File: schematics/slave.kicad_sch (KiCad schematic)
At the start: 6 parts, among them SW1 SW_SPDT, U1 LF33_TO220, U2 ESP32-C6-DevKitC-1

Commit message: add a backup ir sensor
Signed-off-by: zayats1 <zaiats.bogdan@gmail.com>
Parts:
- added U3: IRM-H6xxT, OptoDevice:Everlight_IRM-H6xxT, symbol Interface_Optical:IRM-H6xxT
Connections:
- net +3.3V: now also U3.4 (Vcc)
- net at U2.23 (GPIO18): now also U3.3 (OUT)
- net at U2.32 (GND): now also U3.1 (GND), U3.2 (GND)
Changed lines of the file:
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@@
+	(wire
+		(pts
+			(xy 193.04 86.36) (xy 185.42 86.36)
+		)
+		(stroke
+			(width 0)
+			(type default)
+		)
+	)
 	(wire
 		(pts
@@
 	(wire
 		(pts
+			(xy 182.88 62.23) (xy 182.88 66.04)
+		)
+		(stroke
+			(width 0)
+			(type default)
+		)
+	)
+	(wire
+		(pts
 			(xy 142.24 43.18) (xy 127 43.18)
 		)
@@
 	(wire
 		(pts
+			(xy 182.88 71.12) (xy 207.01 71.12)
+		)
+		(stroke
+			(width 0)
+			(type default)
+		)
+	)
+	(wire
+		(pts
 			(xy 161.29 29.21) (xy 161.29 34.29)
 		)
@@
 	(wire
 		(pts
+			(xy 207.01 109.22) (xy 185.42 109.22)
+		)
+		(stroke
+			(width 0)
+			(type default)
+		)
+	)
+	(wire
+		(pts
+			(xy 182.88 76.2) (xy 193.04 76.2)
+		)
+		(stroke
+			(width 0)
+			(type default)
+		)
+	)
+	(wire
+		(pts
 			(xy 127 121.92) (xy 134.62 121.92)
 		)
@@
 	(wire
 		(pts
+			(xy 193.04 76.2) (xy 193.04 86.36)
+		)
+		(stroke
+			(width 0)
+			(type default)
+		)
+	)
+	(wire
+		(pts
 			(xy 161.29 41.91) (xy 161.29 43.18)
 		)
@@
 		(pts
 			(xy 127 128.27) (xy 127 121.92)
+		)
+		(stroke
+			(width 0)
+			(type default)
+		)
+	)
+	(wire
+		(pts
+			(xy 207.01 71.12) (xy 207.01 109.22)
 		)
 		(stroke
@@
 	)
 	(symbol
+		(lib_id "Interface_Optical:IRM-H6xxT")
+		(at 172.72 71.12 0)
+		(unit 1)
+		(exclude_from_sim no)
+		(in_bom yes)
+		(on_board yes)
+		(dnp no)
+		(fields_autoplaced yes)
+		(property "Reference" "U3"
+			(at 170.985 59.69 0)
+			(effects
+				(font
+					(size 1.27 1.27)
+				)
+			)
+		)
+		(property "Value" "IRM-H6xxT"
+			(at 170.985 62.23 0)
+			(effects
+				(font
+					(size 1.27 1.27)
+				)
+			)
+		)
+		(property "Footprint" "OptoDevice:Everlight_IRM-H6xxT"
+			(at 171.45 80.645 0)
+			(effects
+				(font
+					(size 1.27 1.27)
+				)
+				(hide yes)
+			)
+		)
+		(property "Datasheet" "https://en.everlight.com/wp-content/plugins/ItemRelationship/product_files/pdf/DMO-0000004-IRM-H6XX-TR2_Series_Datasheet_V4.pdf"
+			(at 189.23 63.5 0)
+			(effects
+				(font
+					(size 1.27 1.27)
+				)
+				(hide yes)
+			)
+		)
+		(property "Description" "IR Receiver Modules for remote controls"
+			(at 172.72 71.12 0)
+			(effects
+				(font
+					(size 1.27 1.27)
+				)
+				(hide yes)
+			)
+		)
+		(pin "3"
+		)
+		(pin "1"
+		)
+		(pin "2"
+		)
+		(pin "4"
+		)
+		(instances
+			(project ""
+				(path "/b33adb57-441b-4653-995a-012b7a2cdd51"
+					(reference "U3")
+					(unit 1)
+				)
+			)
+		)
+	)
+	(symbol
 		(lib_id "power:+3.3V")
 		(at 123.19 66.04 0)
@@
 					(unit 1)
 				)
+			)
+		)
+	)
+	(symbol
+		(lib_id "power:+3.3V")
+		(at 182.88 62.23 0)
+		(unit 1)
+		(exclude_from_sim no)
+		(in_bom yes)
+		(on_board yes)
+		(dnp no)
+		(fields_autoplaced yes)
+		(property "Reference" "#PWR02"
+			(at 182.88 66.04 0)
+			(effects
+				(font
+					(size 1.27 1.27)
+				)
+				(hide yes)
+			)
+		)
+		(property "Value" "+3.3V"
+			(at 182.88 57.15 0)
+			(effects
+				(font
+					(size 1.27 1.27)
+				)
+			)
+		)
+		(property "Footprint" ""
+			(at 182.88 62.23 0)
+			(effects
+				(font
+					(size 1.27 1.27)
+				)
+				(hide yes)
+			)
+		)
+		(property "Datasheet" ""
+			(at 182.88 62.23 0)
+			(effects
+				(font
+					(size 1.27 1.27)
+				)
+				(hide yes)
+			)
+		)
+		(property "Description" "Power symbol creates a global label with name \"+3.3V\""
+			(at 182.88 62.23 0)
+			(effects
+				(font
+					(size 1.27 1.27)
+				)
+				(hide yes)
+			)
+		)
+		(pin "1"
+		)
+		(instances
+			(project ""
+				(path "/b33adb57-441b-4653-995a-012b7a2cdd51"
+					(reference "#PWR02")
+					(unit 1)
+				)

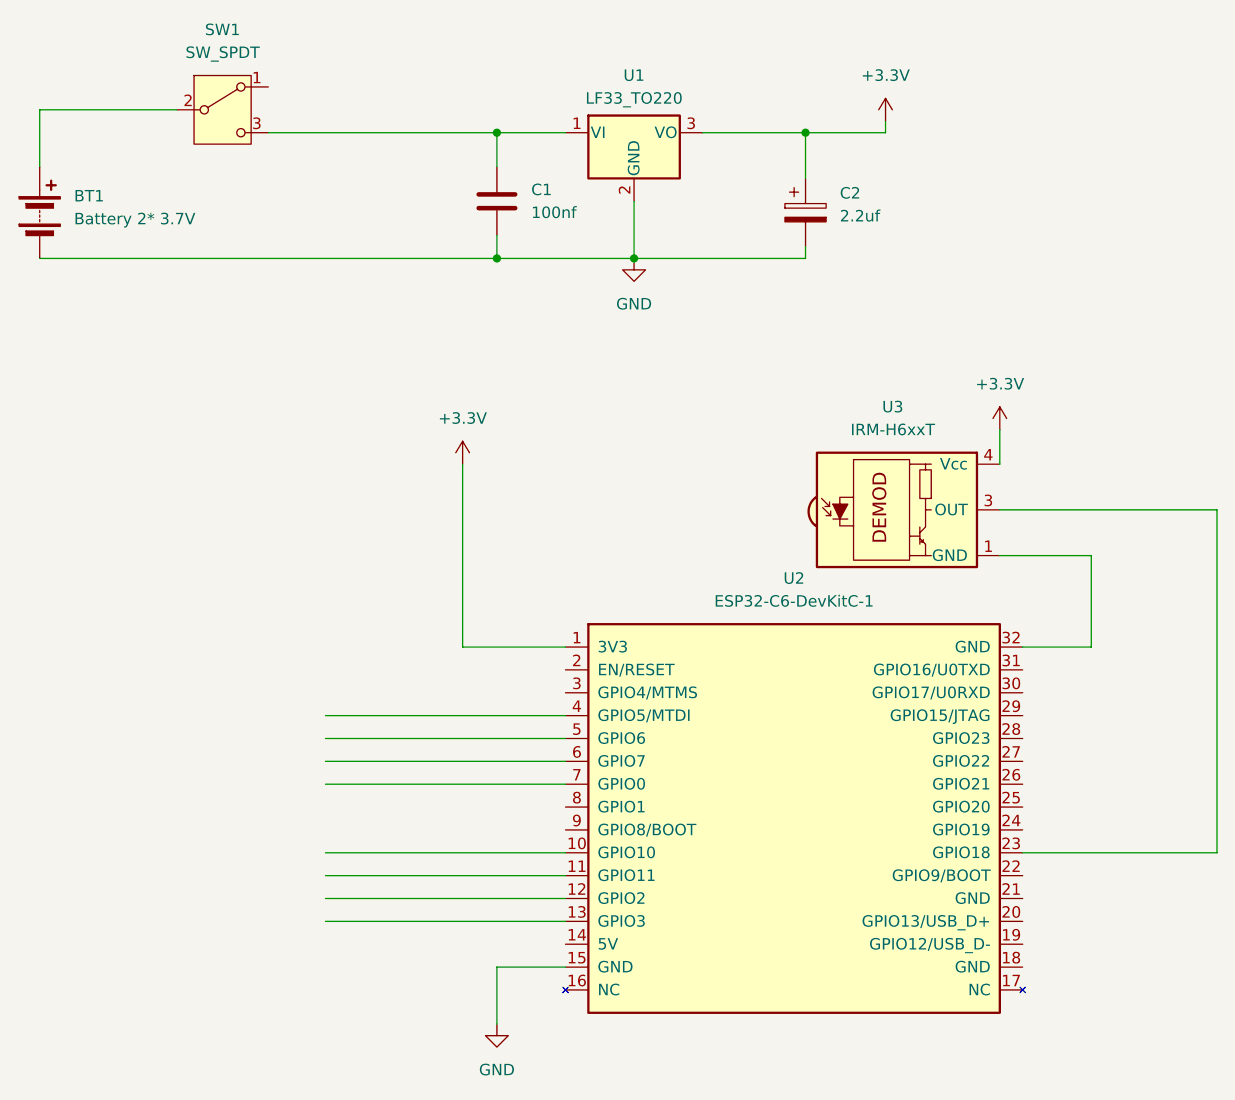
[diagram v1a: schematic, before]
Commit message: change voltage regulator IC to AMS1117-3.3 module
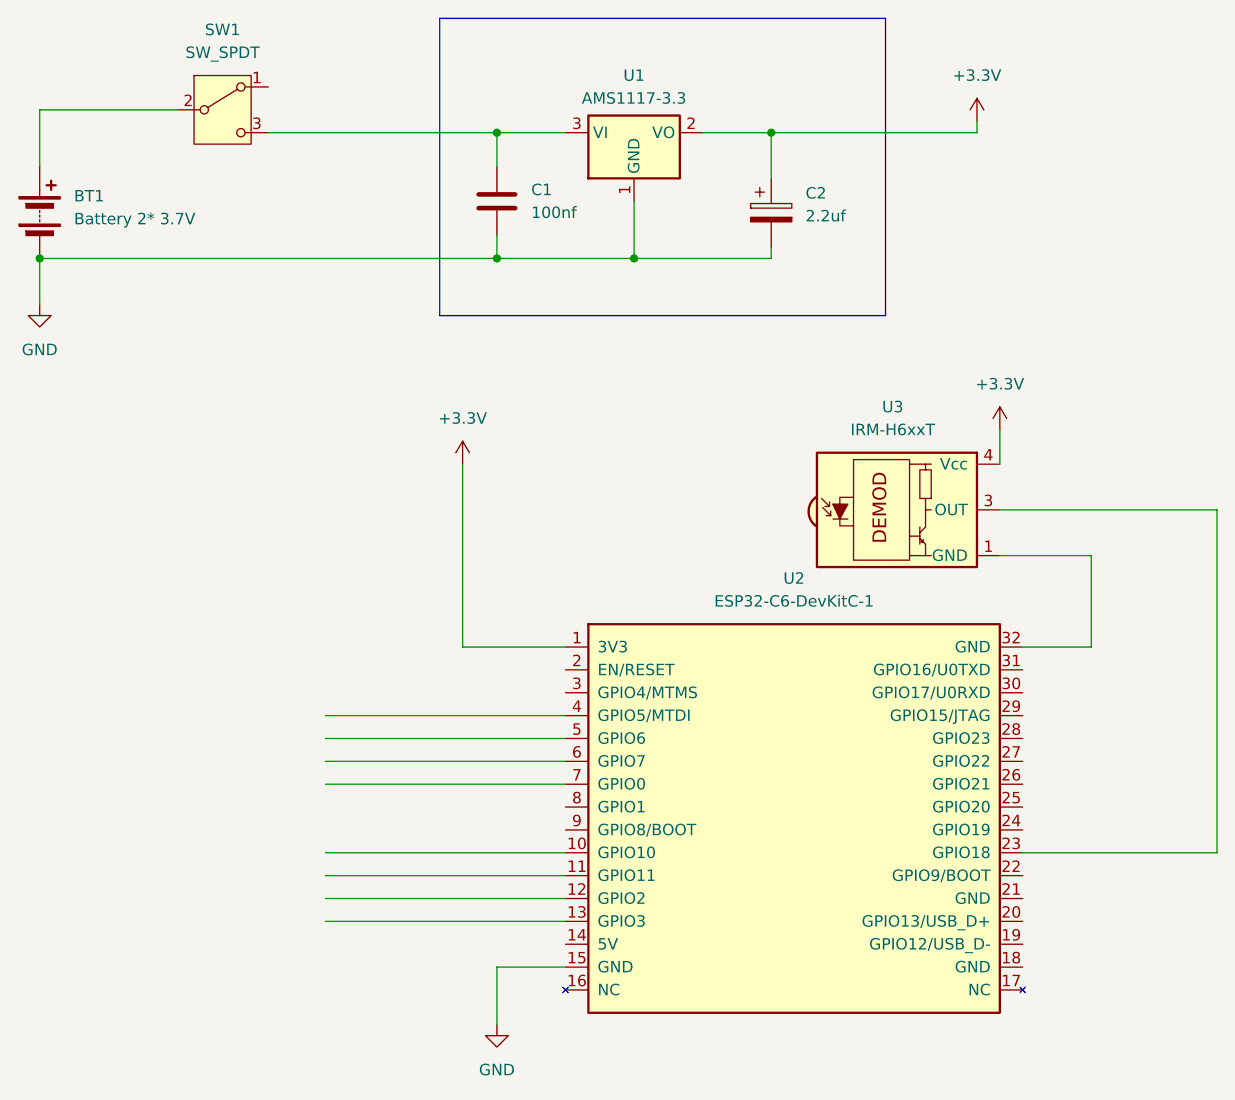
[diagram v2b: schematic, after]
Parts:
- removed U1: LF33_TO220, Package_TO_SOT_THT:TO-220-3_Vertical, symbol Regulator_Linear:LF33_TO220
- added U1: AMS1117-3.3, Package_TO_SOT_SMD:SOT-223-3_TabPin2, symbol Regulator_Linear:AMS1117-3.3
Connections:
- net +3.3V: now also U1.2 (VO)
- net GND: now also U1.1 (GND)
- net at C1.1, SW1.3 (C): now also U1.3 (VI)
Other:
- moved on the sheet: C2
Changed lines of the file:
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@@
 	(generator_version "9.0")
 	(paper "A4")
+	(rectangle
+		(start 120.65 16.51)
+		(end 170.18 49.53)
+		(stroke
+			(width 0)
+			(type default)
+		)
+		(fill
+			(type none)
+		)
+	)
 	(junction
-		(at 161.29 29.21)
+		(at 76.2 43.18)
 		(diameter 0)
 		(color 0 0 0 0)
@@
 		(color 0 0 0 0)
 	)
+	(junction
+		(at 157.48 29.21)
+		(diameter 0)
+		(color 0 0 0 0)
+	)
 	(wire
 		(pts
@@
 	(wire
 		(pts
+			(xy 76.2 43.18) (xy 76.2 48.26)
+		)
+		(stroke
+			(width 0)
+			(type default)
+		)
+	)
+	(wire
+		(pts
 			(xy 107.95 109.22) (xy 134.62 109.22)
 		)
@@
 	(wire
 		(pts
+			(xy 157.48 29.21) (xy 180.34 29.21)
+		)
+		(stroke
+			(width 0)
+			(type default)
+		)
+	)
+	(wire
+		(pts
 			(xy 76.2 26.67) (xy 91.44 26.67)
 		)
@@
 	(wire
 		(pts
-			(xy 161.29 29.21) (xy 170.18 29.21)
-		)
-		(stroke
-			(width 0)
-			(type default)
-		)
-	)
-	(wire
-		(pts
 			(xy 107.95 114.3) (xy 134.62 114.3)
 		)
@@
 	(wire
 		(pts
+			(xy 76.2 43.18) (xy 127 43.18)
+		)
+		(stroke
+			(width 0)
+			(type default)
+		)
+	)
+	(wire
+		(pts
 			(xy 182.88 71.12) (xy 207.01 71.12)
 		)
@@
 	(wire
 		(pts
-			(xy 161.29 29.21) (xy 161.29 34.29)
+			(xy 157.48 29.21) (xy 157.48 34.29)
 		)
 		(stroke
@@
 	(wire
 		(pts
-			(xy 142.24 43.18) (xy 161.29 43.18)
-		)
-		(stroke
-			(width 0)
-			(type default)
-		)
-	)
-	(wire
-		(pts
-			(xy 170.18 29.21) (xy 170.18 27.94)
+			(xy 142.24 43.18) (xy 157.48 43.18)
+		)
+		(stroke
+			(width 0)
+			(type default)
+		)
+	)
+	(wire
+		(pts
+			(xy 180.34 29.21) (xy 180.34 27.94)
 		)
 		(stroke
@@
 	(wire
 		(pts
-			(xy 161.29 41.91) (xy 161.29 43.18)
+			(xy 157.48 41.91) (xy 157.48 43.18)
 		)
 		(stroke
@@
 	(wire
 		(pts
-			(xy 149.86 29.21) (xy 161.29 29.21)
+			(xy 149.86 29.21) (xy 157.48 29.21)
 		)
 		(stroke
@@
 		(pts
 			(xy 76.2 26.67) (xy 76.2 33.02)
-		)
-		(stroke
-			(width 0)
-			(type default)
-		)
-	)
-	(wire
-		(pts
-			(xy 127 43.18) (xy 76.2 43.18)
 		)
 		(stroke
@@
 	)
 	(symbol
+		(lib_id "Regulator_Linear:AMS1117-3.3")
+		(at 142.24 29.21 0)
+		(unit 1)
+		(exclude_from_sim no)
+		(in_bom yes)
+		(on_board yes)
+		(dnp no)
+		(fields_autoplaced yes)
+		(property "Reference" "U1"
+			(at 142.24 22.86 0)
+			(effects
+				(font
+					(size 1.27 1.27)
+				)
+			)
+		)
+		(property "Value" "AMS1117-3.3"
+			(at 142.24 25.4 0)
+			(effects
+				(font
+					(size 1.27 1.27)
+				)
+			)
+		)
+		(property "Footprint" "Package_TO_SOT_SMD:SOT-223-3_TabPin2"
+			(at 142.24 24.13 0)
+			(effects
+				(font
+					(size 1.27 1.27)
+				)
+				(hide yes)
+			)
+		)
+		(property "Datasheet" "http://www.advanced-monolithic.com/pdf/ds1117.pdf"
+			(at 144.78 35.56 0)
+			(effects
+				(font
+					(size 1.27 1.27)
+				)
+				(hide yes)
+			)
+		)
+		(property "Description" "1A Low Dropout regulator, positive, 3.3V fixed output, SOT-223"
+			(at 142.24 29.21 0)
+			(effects
+				(font
+					(size 1.27 1.27)
+				)
+				(hide yes)
+			)
+		)
+		(pin "3"
+		)
+		(pin "1"
+		)
+		(pin "2"
+		)
+		(instances
+			(project ""
+				(path "/b33adb57-441b-4653-995a-012b7a2cdd51"
+					(reference "U1")
+					(unit 1)
+				)
+			)
+		)
+	)
+	(symbol
 		(lib_id "power:GND")
-		(at 142.24 43.18 0)
+		(at 76.2 48.26 0)
 		(unit 1)
 		(exclude_from_sim no)
@@
 		(fields_autoplaced yes)
 		(property "Reference" "#PWR06"
-			(at 142.24 49.53 0)
+			(at 76.2 54.61 0)
 			(effects
 				(font
@@
 		)
 		(property "Value" "GND"
-			(at 142.24 48.26 0)
+			(at 76.2 53.34 0)
 			(effects
 				(font
@@
 		)
 		(property "Footprint" ""
-			(at 142.24 43.18 0)
+			(at 76.2 48.26 0)
 			(effects
 				(font
@@
 		)
 		(property "Datasheet" ""
-			(at 142.24 43.18 0)
+			(at 76.2 48.26 0)
 			(effects
 				(font
@@
 		)
 		(property "Description" "Power symbol creates a global label with name \"GND\" , ground"
-			(at 142.24 43.18 0)
+			(at 76.2 48.26 0)
 			(effects
 				(font
@@
 	(symbol
 		(lib_id "Device:C_Polarized")
-		(at 161.29 38.1 0)
+		(at 157.48 38.1 0)
 		(unit 1)
 		(exclude_from_sim no)
@@
 		(fields_autoplaced yes)
 		(property "Reference" "C2"
-			(at 165.1 35.9409 0)
+			(at 161.29 35.9409 0)
 			(effects
 				(font
@@
 		)
 		(property "Value" "2.2uf"
-			(at 165.1 38.4809 0)
+			(at 161.29 38.4809 0)
 			(effects
 				(font
@@
 		)
 		(property "Footprint" ""
-			(at 162.2552 41.91 0)
+			(at 158.4452 41.91 0)
 			(effects
 				(font
@@
 		)
 		(property "Datasheet" "~"
-			(at 161.29 38.1 0)
+			(at 157.48 38.1 0)
 			(effects
 				(font
@@
 		)
 		(property "Description" "Polarized capacitor"
-			(at 161.29 38.1 0)
+			(at 157.48 38.1 0)
 			(effects
 				(font
@@
 	(symbol
 		(lib_id "power:+3.3V")
-		(at 170.18 27.94 0)
+		(at 180.34 27.94 0)
 		(unit 1)
 		(exclude_from_sim no)
@@
 		(fields_autoplaced yes)
 		(property "Reference" "#PWR07"
-			(at 170.18 31.75 0)
+			(at 180.34 31.75 0)
 			(effects
 				(font
@@
 		)
 		(property "Value" "+3.3V"
-			(at 170.18 22.86 0)
+			(at 180.34 22.86 0)
 			(effects
 				(font
@@
 		)
 		(property "Footprint" ""
-			(at 170.18 27.94 0)
+			(at 180.34 27.94 0)
 			(effects
 				(font
@@
 		)
 		(property "Datasheet" ""
-			(at 170.18 27.94 0)
+			(at 180.34 27.94 0)
 			(effects
 				(font
@@
 		)
 		(property "Description" "Power symbol creates a global label with name \"+3.3V\""
-			(at 170.18 27.94 0)
+			(at 180.34 27.94 0)
 			(effects
 				(font
@@
 					(unit 1)
 				)
-			)
-		)
-	)
-	(symbol
-		(lib_id "Regulator_Linear:LF33_TO220")
-		(at 142.24 29.21 0)
-		(unit 1)
-		(exclude_from_sim no)
-		(in_bom yes)
-		(on_board yes)
-		(dnp no)
-		(fields_autoplaced yes)
-		(property "Reference" "U1"
-			(at 142.24 22.86 0)
-			(effects
-				(font
-					(size 1.27 1.27)
-				)
-			)
-		)
-		(property "Value" "LF33_TO220"
-			(at 142.24 25.4 0)
-			(effects
-				(font
-					(size 1.27 1.27)
-				)
-			)
-		)
-		(property "Footprint" "Package_TO_SOT_THT:TO-220-3_Vertical"
-			(at 142.24 23.495 0)
-			(effects
-				(font
-					(size 1.27 1.27)
-					(italic yes)
-				)
-				(hide yes)
-			)
-		)
-		(property "Datasheet" "http://www.st.com/content/ccc/resource/technical/document/datasheet/c4/0e/7e/2a/be/bc/4c/bd/CD00000546.pdf/files/CD00000546.pdf/jcr:content/translations/en.CD00000546.pdf"
-			(at 142.24 30.48 0)
-			(effects
-				(font
-					(size 1.27 1.27)
-				)
-				(hide yes)
-			)
-		)
-		(property "Description" "Low-drop Voltage Regulator, Io up to 500mA, Fixed Vo 3.3V, TO-220"
-			(at 142.24 29.21 0)
-			(effects
-				(font
-					(size 1.27 1.27)
-				)
-				(hide yes)
-			)
-		)
-		(pin "3"
-		)
-		(pin "2"
-		)
-		(pin "1"
-		)
-		(instances
-			(project ""
-				(path "/b33adb57-441b-4653-995a-012b7a2cdd51"
-					(reference "U1")
-					(unit 1)
-				)

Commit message: changed motor outputs from boot pins to normal
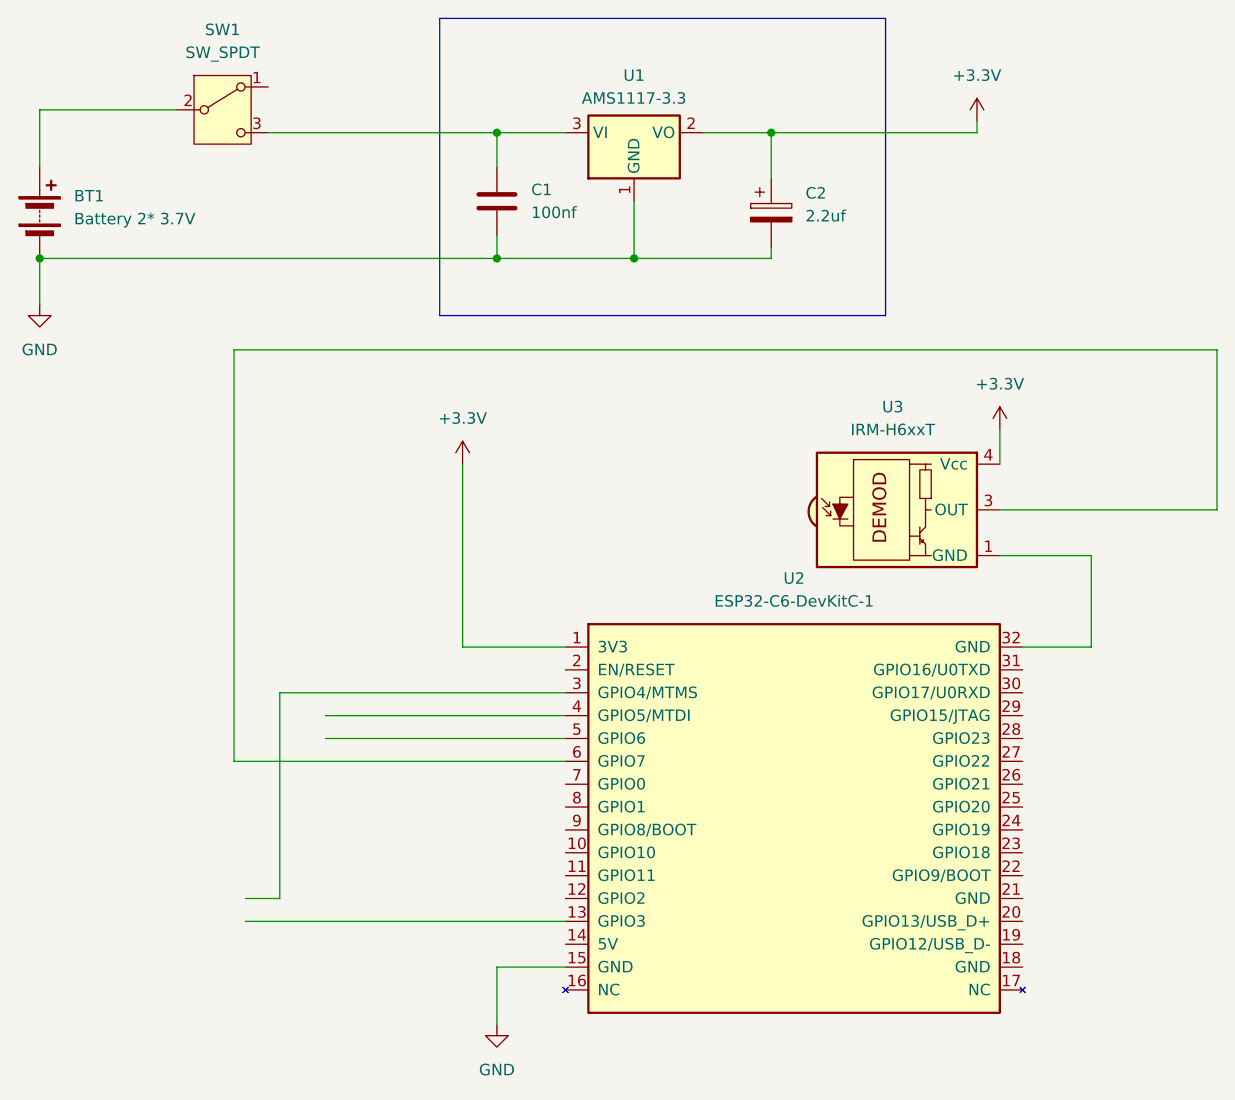
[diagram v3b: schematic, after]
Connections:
- net at U3.3 (OUT): now also U2.6 (GPIO7); no longer U2.23 (GPIO18)
